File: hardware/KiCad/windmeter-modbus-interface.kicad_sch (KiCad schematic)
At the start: 4 parts, among them U1 CH32V003J4M6, U2 MAX3485, U3 CH32V003A4M6, U4 CH32V003F4P6

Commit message: Update PCB
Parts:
- removed U3: CH32V003A4M6, Package_SO:STC_SOP-16_3.9x9.9mm_P1.27mm, symbol MCU_WCH_RiscV:CH32V003AxMx
- removed U4: CH32V003F4P6, Package_SO:TSSOP-20_4.4x6.5mm_P0.65mm, symbol MCU_WCH_RiscV:CH32V003FxPx
- added C1, C2: 100n, Capacitor_SMD:C_1206_3216Metric_Pad1.33x1.80mm_HandSolder, symbol Device:C
- added D1: SM712_SOT23, Package_TO_SOT_SMD:SOT-23, symbol Diode:SM712_SOT23
- added J1: MODBUS-P1, my-KiCad-library:CONN_215877-1, symbol my-KiCad-library:215877-1
- added J2: Programming, Connector_PinHeader_2.54mm:PinHeader_1x03_P2.54mm_Vertical, symbol Connector:Conn_01x03_Pin
- added J3: MODBUS-P2, my-KiCad-library:CONN_215877-1, symbol my-KiCad-library:215877-1
- added JP1: enable term., Jumper:SolderJumper-2_P1.3mm_Open_Pad1.0x1.5mm, symbol Jumper:SolderJumper_2_Open
- added JP2, JP3, JP4, JP5: (no value), Jumper:SolderJumper-3_P1.3mm_Bridged12_Pad1.0x1.5mm_NumberLabels, symbol SparkFun-Jumper:SolderJumper_3_Bridged12
- added JP6: Address select, Jumper:SolderJumper-2_P1.3mm_Open_Pad1.0x1.5mm, symbol Jumper:SolderJumper_2_Open
- added R1: 120, Resistor_SMD:R_1206_3216Metric_Pad1.30x1.75mm_HandSolder, symbol Device:R
- added R2, R3: 20k, Resistor_SMD:R_1206_3216Metric_Pad1.30x1.75mm_HandSolder, symbol Device:R
- added R4: 10k, Resistor_SMD:R_1206_3216Metric_Pad1.30x1.75mm_HandSolder, symbol Device:R
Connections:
- net MB-TX/RX: now reaches U1.1 (PD6/PA1)
- net MB-TX/RX: now also U2.1 (RO), U2.4 (DI)
- net GND: now reaches U1.2 (VSS)
- net GND: now also U2.5 (GND), C1.2, C2.2, D1.3 (common), J1.7 (8), J1.8 (7), J2.1 (Pin_1), J3.7 (8), J3.8 (7), JP6.1 (A), R2.2
- net ANALOG_IN: now reaches U1.3 (PA2)
- net 3V3: now reaches U1.4 (VDD)
- net 3V3: now also U2.8 (VCC), C1.1, C2.1, J2.3 (Pin_3), R3.1, R4.2
- net PULSE_IN: now reaches U1.5 (PC1)
- net MB-RE/DE: now reaches U1.6 (PC2)
- net MB-RE/DE: now also U2.2 (~{RE}), U2.3 (DE)
- net ADDRESS: now reaches U1.7 (PC4)
- net ADDRESS: now also JP6.2 (B), R4.1
- net SWIO: now reaches U1.8 (PD1/PD4/PD5)
- net SWIO: now also J2.2 (Pin_2)
- net RS485-A: now reaches U2.6 (A)
- net RS485-A: now also D1.1 (A1), JP1.2 (B), JP3.2 (B), JP5.2 (B), R3.2
- net RS485-B: now reaches U2.7 (B)
- net RS485-B: now also D1.2 (A2), JP2.2 (B), JP4.2 (B), R1.2, R2.1
- new net: JP1.1 (A), R1.1
- new net 24V: J1.4 (3), J1.5 (6), J3.4 (3), J3.5 (6)
- new net Aa: J1.6 (5), JP2.1 (A)
- new net Ab: J1.2 (1), JP2.3 (C)
- new net Ba: J1.3 (4), JP3.1 (A)
- new net Bb: J1.1 (2), JP3.3 (C)
- new net _Aa: J3.6 (5), JP4.1 (A)
- new net _Ab: J3.2 (1), JP4.3 (C)
- new net _Ba: J3.3 (4), JP5.1 (A)
- new net _Bb: J3.1 (2), JP5.3 (C)
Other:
- moved on the sheet: U1, U2

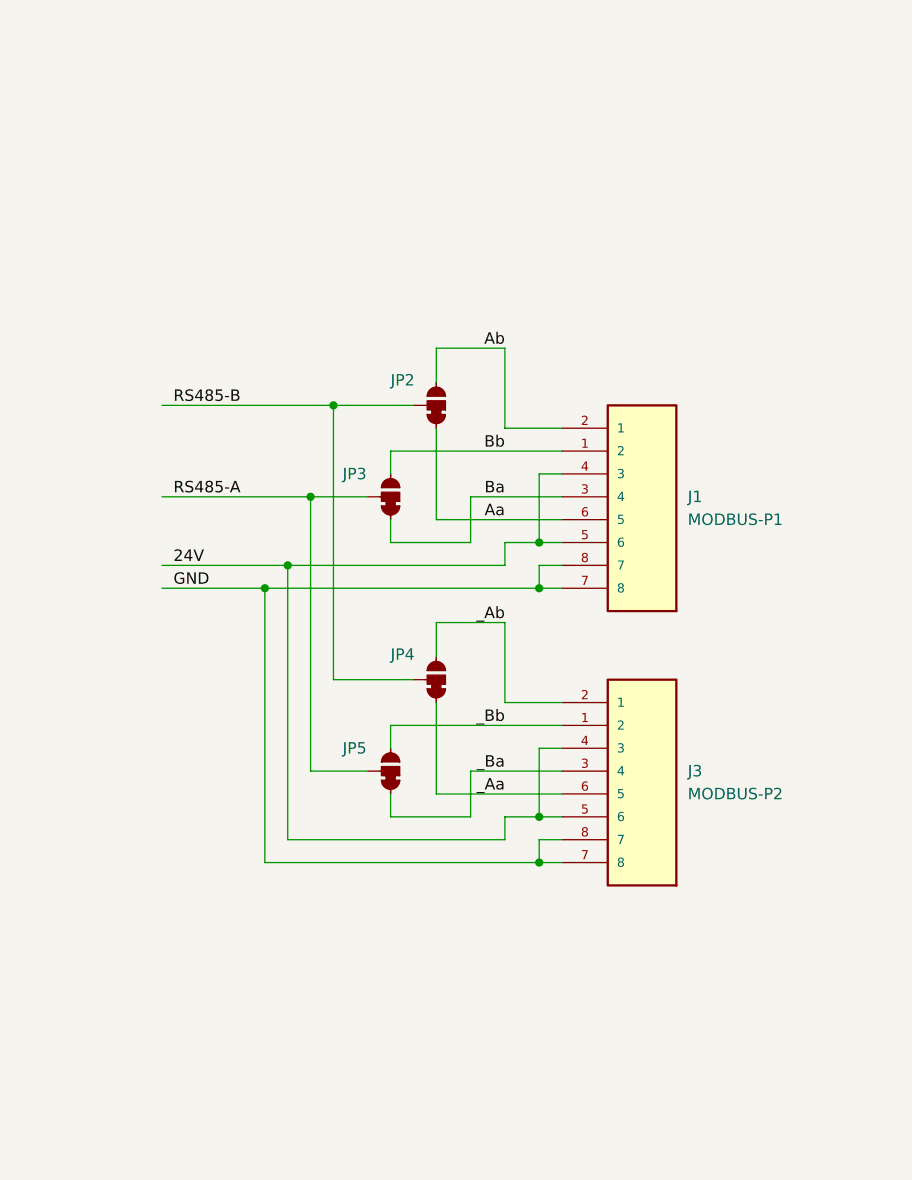
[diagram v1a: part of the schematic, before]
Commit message: Added power circuit
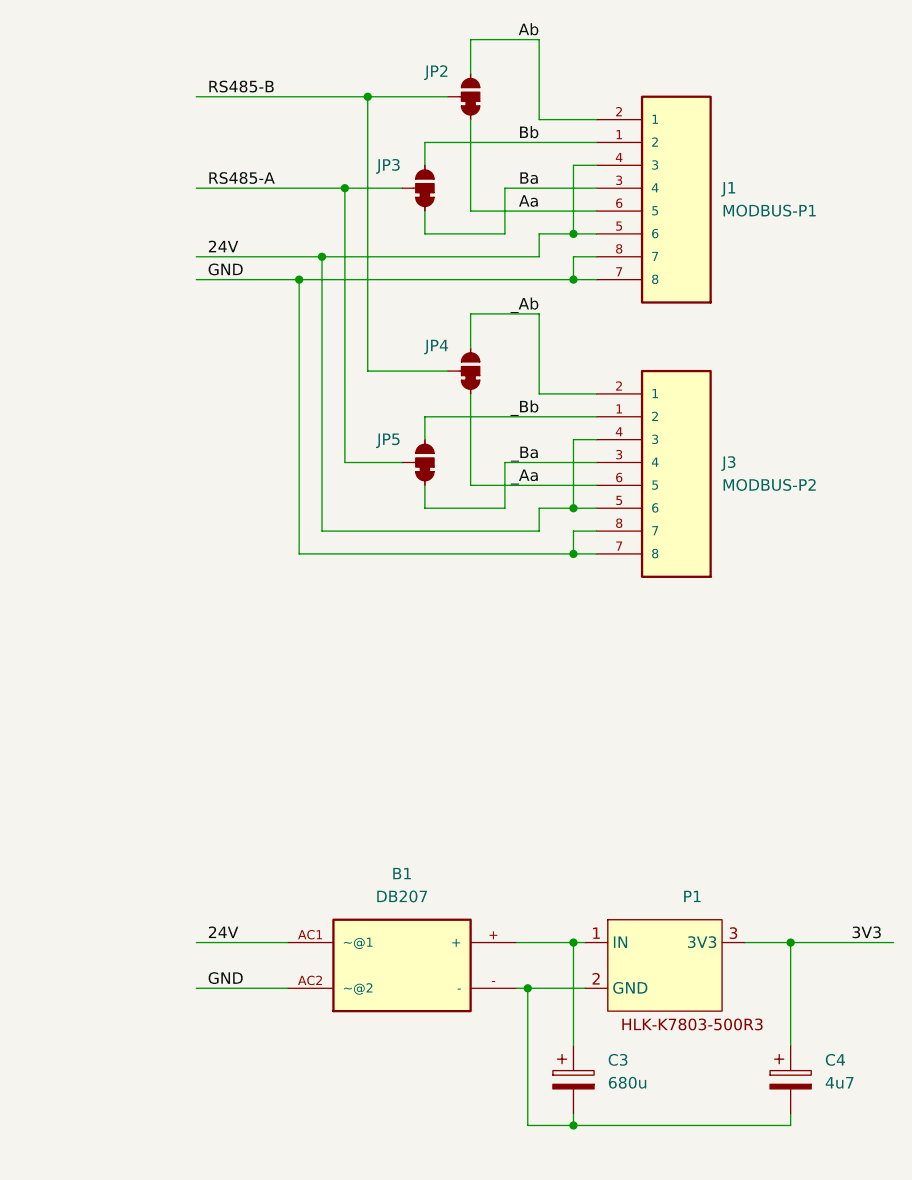
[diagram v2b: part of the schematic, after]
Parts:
- added B1: DB207, DB207:DB207, symbol my-KiCad-library:DB207
- added C3: 680u, symbol Device:C_Polarized
- added C4: 4u7, symbol Device:C_Polarized
- added P1: (no value), symbol my-KiCad-library:HLK-K7803-500R3
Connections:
- net 24V: now also B1.AC1 (~@1)
- net 3V3: now also C4.1, P1.3 (3V3)
- net GND: now also B1.AC2 (~@2)
- new net: B1.-, C3.2, C4.2, P1.2 (GND)
- new net: B1.+, C3.1, P1.1 (IN)
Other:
- moved on the sheet: J1, J3, JP2, JP3, JP4, JP5

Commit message: First scaffolding
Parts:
- added C5: 100n, Capacitor_SMD:C_1206_3216Metric_Pad1.33x1.80mm_HandSolder, symbol Device:C
- added D2: BZX84Cxx, Package_TO_SOT_SMD:SOT-23, symbol Diode:BZX84Cxx
- added J4: RJ14, symbol Connector:RJ14
- added R5: 10k, Resistor_SMD:R_1206_3216Metric_Pad1.30x1.75mm_HandSolder, symbol Device:R
- added R6: 100, Resistor_SMD:R_1206_3216Metric_Pad1.30x1.75mm_HandSolder, symbol Device:R
- C3: value 680u -> 100u
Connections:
- net 3V3: now also J4.1, R5.2
- net ANALOG_IN: now also J4.4
- net GND: now also C5.1, D2.1 (A), J4.3
- net PULSE_IN: now also C5.2, D2.3 (K), R5.1, R6.1
- new net: J4.2, R6.2
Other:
- company: (none) -> RFSee
- title: (none) -> Windmeter interface for Modbus RS458
- moved on the sheet: B1, C1, C2, C3, C4, D1, J2, JP1, JP6, P1, R1, R2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
